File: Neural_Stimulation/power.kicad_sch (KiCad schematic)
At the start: 16 parts, among them U3 LTC3035EDDBPBF, U4 LTC3035EDDBPBF

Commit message: Added level shifters
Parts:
- added C26: 0.1uF, symbol Device:C
- added R24: 100, symbol Device:R
- added R25: 50m, symbol Device:R
- added R27: 10k, symbol Device:R
- added R28: 500m, symbol Device:R
- added U5: LT6106, Package_TO_SOT_SMD:SOT-23-5, symbol Amplifier_Current:LT6106
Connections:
- net GND: now also C26.2, R27.1, U5.2 (V-)
- net +3V3: now reaches C25.1, R20.1, U4.5 (OUT)
- net +1V8: now reaches C23.1, R22.1, U3.5 (OUT)
- new net: R24.1, R25.1, R28.1, U5.5 (V+)
- new net: C26.1, R25.2, R28.2, U5.4 (+)
- new net: R24.2, U5.3 (-)
- new net VDD_ISENSE: R27.2, U5.1
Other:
- note added: "LDO GENERATING VDD FOR CSI040"
- note added: "LDO GENERATING VDD FOR MCU"
- moved on the sheet: C23, R22

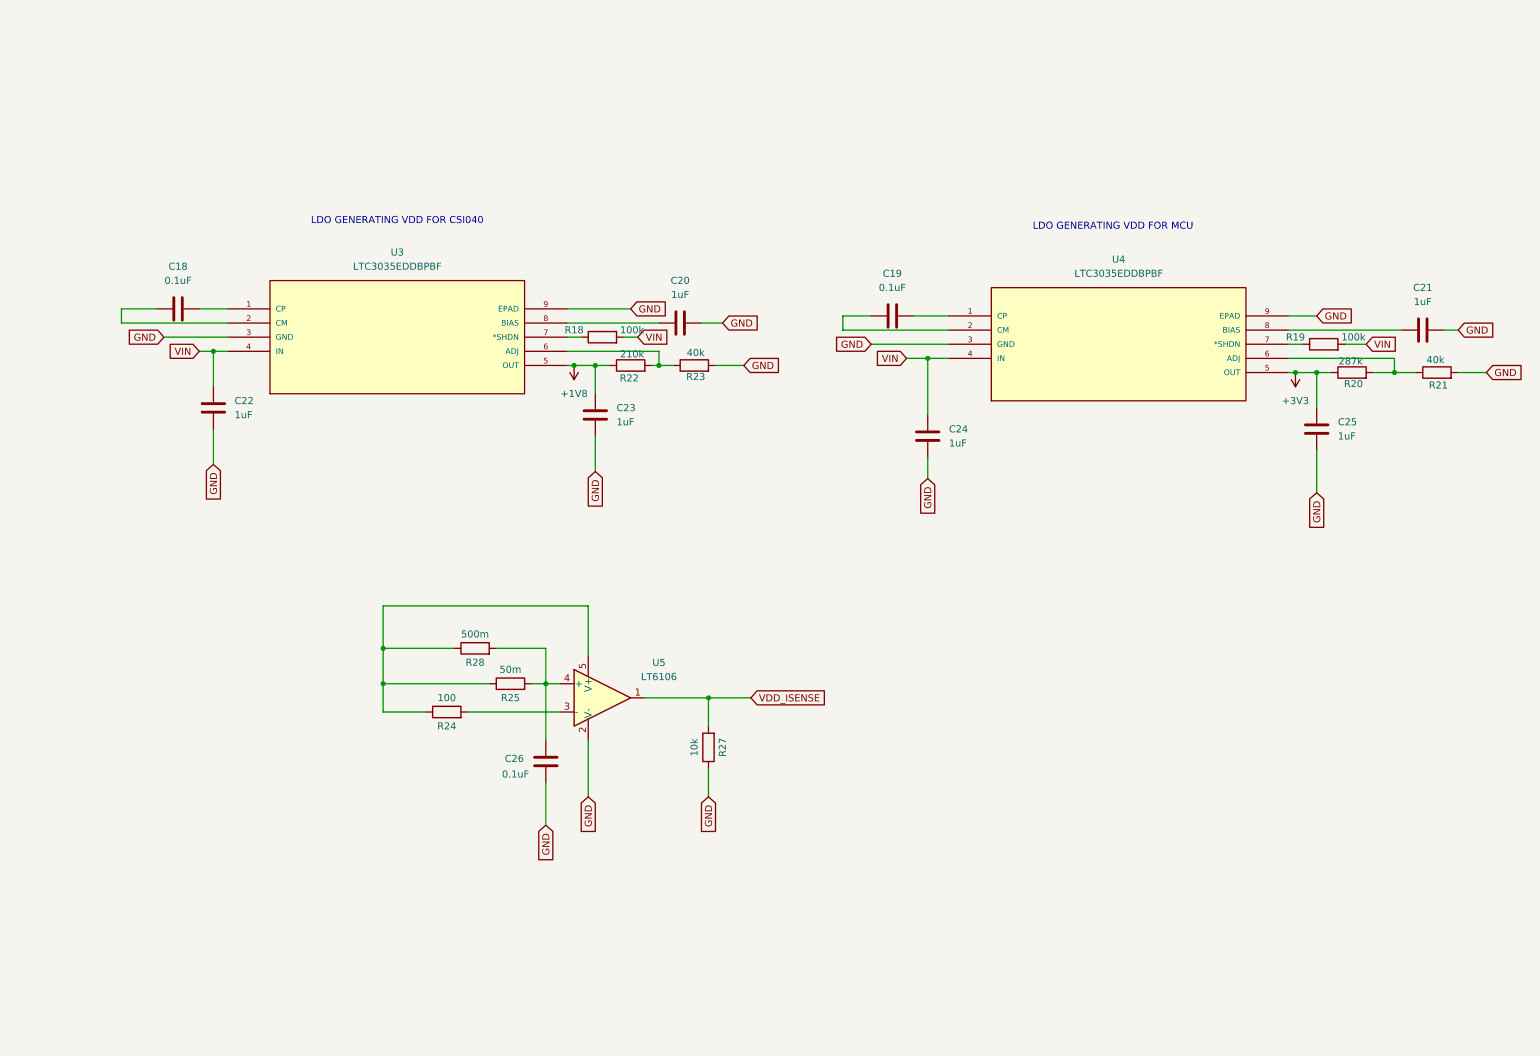
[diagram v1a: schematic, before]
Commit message: Added boost converter for generating VMAX
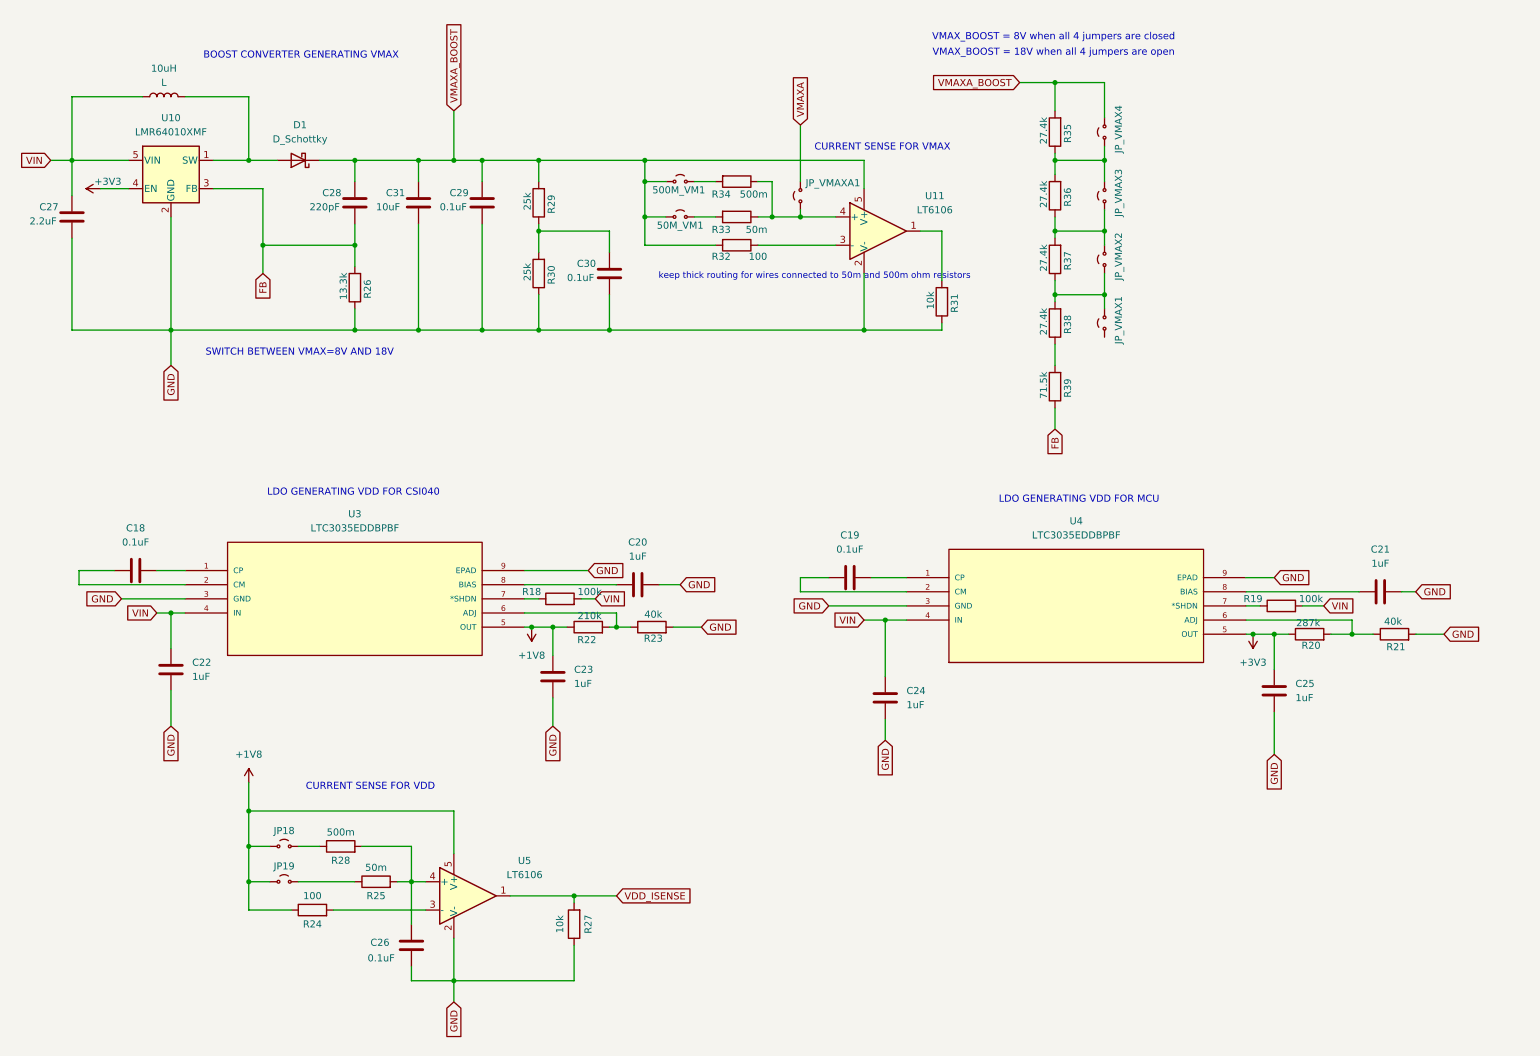
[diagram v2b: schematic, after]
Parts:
- added 10uH: L, symbol Device:L
- added 500M_VM1, 50M_VM1, JP18, JP19, JP_VMAX1, JP_VMAX2, JP_VMAX3, JP_VMAX4, JP_VMAXA1: Jumper_2_Small_Open, symbol Jumper:Jumper_2_Small_Open
- added C27: 2.2uF, symbol Device:C
- added C28: 220pF, symbol Device:C
- added C29, C30: 0.1uF, symbol Device:C
- added C31: 10uF, symbol Device:C
- added D1: D_Schottky, symbol Device:D_Schottky
- added R26: 13.3k, symbol Device:R
- added R29, R30: 25k, symbol Device:R
- added R31: 10k, symbol Device:R
- added R32: 100, symbol Device:R
- added R33: 50m, symbol Device:R
- added R34: 500m, symbol Device:R
- added R35, R36, R37, R38: 27.4k, symbol Device:R
- added R39: 71.5k, symbol Device:R
- added U10: LMR64010XMF, Package_TO_SOT_SMD:SOT-23-5, symbol Regulator_Switching:LMR64010XMF
- added U11: LT6106, Package_TO_SOT_SMD:SOT-23-5, symbol Amplifier_Current:LT6106
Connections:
- net +1V8: now also R24.1, U5.5 (V+), JP18.1 (A), JP19.1 (A)
- net +3V3: now also U10.4 (EN)
- net GND: now also C27.1, C29.1, C30.1, C31.1, R26.1, R30.1, R31.1, U10.2 (GND), U11.2 (V-)
- net VIN: now also 10uH.1, C27.2, U10.5 (VIN)
- new net: C30.2, R29.1, R30.2
- new net: JP_VMAXA1.1 (A), R33.1, R34.1, U11.4 (+)
- new net: 50M_VM1.2 (B), R33.2
- new net: JP_VMAX3.2 (B), JP_VMAX4.1 (A), R35.1, R36.2
- new net: JP_VMAX1.2 (B), JP_VMAX2.1 (A), R37.1, R38.2
- new net: R31.2, U11.1
- new net: 500M_VM1.2 (B), R34.2
- new net: JP18.2 (B), R28.1
- new net: 10uH.2, D1.2 (A), U10.1 (SW)
- new net: JP_VMAX2.2 (B), JP_VMAX3.1 (A), R36.1, R37.2
- new net: R38.1, R39.2
- new net: JP19.2 (B), R25.1
- new net: R32.1, U11.3 (-)
- new net FB: C28.1, R26.2, R39.1, U10.3 (FB)
- new net VMAXA: JP_VMAXA1.2 (B)
- new net VMAXA_BOOST: 500M_VM1.1 (A), 50M_VM1.1 (A), C28.2, C29.2, C31.2, D1.1 (K), JP_VMAX4.2 (B), R29.2, R32.2, R35.2, U11.5 (V+)
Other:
- note added: "BOOST CONVERTER GENERATING VMAX"
- note added: "CURRENT SENSE FOR VDD"
- note added: "CURRENT SENSE FOR VMAX"
- note added: "SWITCH BETWEEN VMAX=8V AND 18V"
- note added: "VMAX_BOOST = 18V when all 4 jumpers are open"
- note added: "VMAX_BOOST = 8V when all 4 jumpers are closed"
- note added: "keep thick routing for wires connected to 50m and 500m ohm resistors"
- moved on the sheet: C18, C19, C20, C21, C22, C23, C24, C25, C26, R18, R19, R20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

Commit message: Added VREF Connections
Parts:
- added JP_VREFA: Jumper_2_Small_Open, symbol Jumper:Jumper_2_Small_Open
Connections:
- net at C30.2, R29.1, R30.2: now also JP_VREFA.2 (B)
- new net VREF_A: JP_VREFA.1 (A)
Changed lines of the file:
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@@
 	)
 	(junction
+		(at 119.38 50.8)
+		(diameter 0)
+		(color 0 0 0 0)
+	)
+	(junction
 		(at 96.52 68.58)
 		(diameter 0)
@@
 	(wire
 		(pts
+			(xy 119.38 31.75) (xy 119.38 41.91)
+		)
+		(stroke
+			(width 0)
+			(type default)
+		)
+	)
+	(wire
+		(pts
 			(xy 19.05 38.1) (xy 22.86 38.1)
 		)
@@
 	(wire
 		(pts
+			(xy 119.38 46.99) (xy 119.38 50.8)
+		)
+		(stroke
+			(width 0)
+			(type default)
+		)
+	)
+	(wire
+		(pts
 			(xy 30.48 111.76) (xy 24.13 111.76)
 		)
@@
 	(wire
 		(pts
-			(xy 119.38 50.8) (xy 106.68 50.8)
+			(xy 106.68 50.8) (xy 119.38 50.8)
 		)
 		(stroke
@@
 		)
 	)
+	(global_label "VREF_A"
+		(shape input)
+		(at 119.38 31.75 90)
+		(fields_autoplaced yes)
+		(effects
+			(font
+				(size 1.27 1.27)
+			)
+			(justify left)
+		)
+		(property "Intersheetrefs" "${INTERSHEET_REFS}"
+			(at 119.38 22.1124 90)
+			(effects
+				(font
+					(size 1.27 1.27)
+				)
+				(justify left)
+				(hide yes)
+			)
+		)
+	)
 	(global_label "GND"
 		(shape input)
@@
 					(unit 1)
 				)
+			)
+		)
+	)
+	(symbol
+		(lib_id "Jumper:Jumper_2_Small_Open")
+		(at 119.38 44.45 270)
+		(unit 1)
+		(exclude_from_sim yes)
+		(in_bom yes)
+		(on_board yes)
+		(dnp no)
+		(property "Reference" "JP_VREFA"
+			(at 122.174 44.45 0)
+			(effects
+				(font
+					(size 1.27 1.27)
+				)
+			)
+		)
+		(property "Value" "Jumper_2_Small_Open"
+			(at 123.19 44.45 0)
+			(effects
+				(font
+					(size 1.27 1.27)
+				)
+				(hide yes)
+			)
+		)
+		(property "Footprint" ""
+			(at 119.38 44.45 0)
+			(effects
+				(font
+					(size 1.27 1.27)
+				)
+				(hide yes)
+			)
+		)
+		(property "Datasheet" "~"
+			(at 119.38 44.45 0)
+			(effects
+				(font
+					(size 1.27 1.27)
+				)
+				(hide yes)
+			)
+		)
+		(property "Description" "Jumper, 2-pole, small symbol, open"
+			(at 119.38 44.45 0)
+			(effects
+				(font
+					(size 1.27 1.27)
+				)
+				(hide yes)
+			)
+		)
+		(pin "1"
+		)
+		(pin "2"
+		)
+		(instances
+			(project "NeuralStimBoard.kicad_sym"
+				(path "/0df850d8-90a2-4d89-b281-e26bc82d6cd9/2af15af9-f56a-408a-9186-69deac584b7e"
+					(reference "JP_VREFA")
+					(unit 1)
+				)

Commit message: Added VDD connections to CSI040
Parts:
- added JP_VDD: Jumper_2_Small_Open, symbol Jumper:Jumper_2_Small_Open
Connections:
- net at C26.1, R25.2, R28.2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: now also JP_VDD.1 (A)
- new net VDD: JP_VDD.2 (B)
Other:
- moved on the sheet: C26, R25
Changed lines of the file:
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@@
 	)
 	(junction
+		(at 82.55 167.64)
+		(diameter 0)
+		(color 0 0 0 0)
+	)
+	(junction
+		(at 85.09 167.64)
+		(diameter 0)
+		(color 0 0 0 0)
+	)
+	(junction
+		(at 54.61 151.13)
+		(diameter 0)
+		(color 0 0 0 0)
+	)
+	(junction
 		(at 22.86 38.1)
 		(diameter 0)
@@
 	)
 	(junction
-		(at 83.82 167.64)
-		(diameter 0)
-		(color 0 0 0 0)
-	)
-	(junction
 		(at 234.95 123.19)
 		(diameter 0)
@@
 	)
 	(junction
-		(at 54.61 154.94)
-		(diameter 0)
-		(color 0 0 0 0)
-	)
-	(junction
 		(at 85.09 68.58)
 		(diameter 0)
@@
 	(wire
 		(pts
-			(xy 91.44 185.42) (xy 83.82 185.42)
+			(xy 91.44 185.42) (xy 82.55 185.42)
 		)
 		(stroke
@@
 	(wire
 		(pts
-			(xy 54.61 149.86) (xy 54.61 154.94)
+			(xy 54.61 146.05) (xy 54.61 151.13)
 		)
 		(stroke
@@
 	(wire
 		(pts
-			(xy 91.44 154.94) (xy 91.44 162.56)
+			(xy 91.44 151.13) (xy 91.44 162.56)
 		)
 		(stroke
@@
 	(wire
 		(pts
-			(xy 54.61 154.94) (xy 54.61 161.29)
+			(xy 233.68 113.03) (xy 238.76 113.03)
 		)
 		(stroke
@@
 	(wire
 		(pts
-			(xy 233.68 113.03) (xy 238.76 113.03)
+			(xy 166.37 113.03) (xy 172.72 113.03)
 		)
 		(stroke
@@
 	(wire
 		(pts
-			(xy 166.37 113.03) (xy 172.72 113.03)
+			(xy 101.6 170.18) (xy 113.03 170.18)
 		)
 		(stroke
@@
 	(wire
 		(pts
-			(xy 101.6 170.18) (xy 113.03 170.18)
+			(xy 96.52 38.1) (xy 91.44 38.1)
 		)
 		(stroke
@@
 	(wire
 		(pts
-			(xy 96.52 38.1) (xy 91.44 38.1)
+			(xy 54.61 161.29) (xy 54.61 167.64)
 		)
 		(stroke
@@
 	(wire
 		(pts
-			(xy 54.61 161.29) (xy 54.61 167.64)
+			(xy 82.55 167.64) (xy 85.09 167.64)
 		)
 		(stroke
@@
 	(wire
 		(pts
-			(xy 63.5 167.64) (xy 73.66 167.64)
+			(xy 63.5 167.64) (xy 72.39 167.64)
 		)
 		(stroke
@@
 	(wire
 		(pts
+			(xy 54.61 151.13) (xy 54.61 161.29)
+		)
+		(stroke
+			(width 0)
+			(type default)
+		)
+	)
+	(wire
+		(pts
 			(xy 119.38 54.61) (xy 119.38 50.8)
 		)
@@
 	(wire
 		(pts
-			(xy 83.82 167.64) (xy 83.82 175.26)
+			(xy 82.55 167.64) (xy 82.55 175.26)
 		)
 		(stroke
@@
 	(wire
 		(pts
-			(xy 83.82 185.42) (xy 83.82 182.88)
+			(xy 82.55 185.42) (xy 82.55 182.88)
 		)
 		(stroke
@@
 	(wire
 		(pts
-			(xy 83.82 167.64) (xy 86.36 167.64)
+			(xy 134.62 41.91) (xy 138.43 41.91)
 		)
 		(stroke
@@
 	(wire
 		(pts
-			(xy 134.62 41.91) (xy 138.43 41.91)
+			(xy 168.91 130.81) (xy 168.91 120.65)
 		)
 		(stroke
@@
 	(wire
 		(pts
-			(xy 168.91 130.81) (xy 168.91 120.65)
+			(xy 31.75 116.84) (xy 43.18 116.84)
 		)
 		(stroke
@@
 	(wire
 		(pts
-			(xy 31.75 116.84) (xy 43.18 116.84)
+			(xy 130.81 121.92) (xy 135.89 121.92)
 		)
 		(stroke
@@
 	(wire
 		(pts
-			(xy 130.81 121.92) (xy 135.89 121.92)
+			(xy 85.09 161.29) (xy 85.09 167.64)
 		)
 		(stroke
@@
 	(wire
 		(pts
+			(xy 85.09 167.64) (xy 86.36 167.64)
+		)
+		(stroke
+			(width 0)
+			(type default)
+		)
+	)
+	(wire
+		(pts
 			(xy 208.28 30.48) (xy 208.28 24.13)
 		)
@@
 	(wire
 		(pts
-			(xy 74.93 161.29) (xy 83.82 161.29)
+			(xy 74.93 161.29) (xy 82.55 161.29)
 		)
 		(stroke
@@
 	(wire
 		(pts
-			(xy 83.82 161.29) (xy 83.82 167.64)
+			(xy 82.55 161.29) (xy 82.55 167.64)
 		)
 		(stroke
@@
 	(wire
 		(pts
+			(xy 85.09 148.59) (xy 85.09 156.21)
+		)
+		(stroke
+			(width 0)
+			(type default)
+		)
+	)
+	(wire
+		(pts
 			(xy 40.64 68.58) (xy 73.66 68.58)
 		)
@@
 	(wire
 		(pts
-			(xy 54.61 154.94) (xy 91.44 154.94)
+			(xy 54.61 151.13) (xy 91.44 151.13)
 		)
 		(stroke
@@
 	(wire
 		(pts
-			(xy 81.28 167.64) (xy 83.82 167.64)
+			(xy 80.01 167.64) (xy 82.55 167.64)
 		)
 		(stroke
@@
 	(text "CURRENT SENSE FOR VDD"
 		(exclude_from_sim no)
-		(at 76.454 150.622 0)
+		(at 69.596 146.558 0)
 		(effects
 			(font
@@
 		)
 	)
+	(global_label "VDD"
+		(shape input)
+		(at 85.09 148.59 90)
+		(fields_autoplaced yes)
+		(effects
+			(font
+				(size 1.27 1.27)
+			)
+			(justify left)
+		)
+		(property "Intersheetrefs" "${INTERSHEET_REFS}"
+			(at 85.09 141.9762 90)
+			(effects
+				(font
+					(size 1.27 1.27)
+				)
+				(justify left)
+				(hide yes)
+			)
+		)
+	)
 	(global_label "GND"
 		(shape input)
@@
 	)
 	(symbol
+		(lib_id "Jumper:Jumper_2_Small_Open")
+		(at 85.09 158.75 90)
+		(unit 1)
+		(exclude_from_sim yes)
+		(in_bom yes)
+		(on_board yes)
+		(dnp no)
+		(property "Reference" "JP_VDD"
+			(at 79.756 158.242 90)
+			(effects
+				(font
+					(size 1.27 1.27)
+				)
+			)
+		)
+		(property "Value" "Jumper_2_Small_Open"
+			(at 81.28 158.75 0)
+			(effects
+				(font
+					(size 1.27 1.27)
+				)
+				(hide yes)
+			)
+		)
+		(property "Footprint" ""
+			(at 85.09 158.75 0)
+			(effects
+				(font
+					(size 1.27 1.27)
+				)
+				(hide yes)
+			)
+		)
+		(property "Datasheet" "~"
+			(at 85.09 158.75 0)
+			(effects
+				(font
+					(size 1.27 1.27)
+				)
+				(hide yes)
+			)
+		)
+		(property "Description" "Jumper, 2-pole, small symbol, open"
+			(at 85.09 158.75 0)
+			(effects
+				(font
+					(size 1.27 1.27)
+				)
+				(hide yes)
+			)
+		)
+		(pin "1"
+		)
+		(pin "2"
+		)
+		(instances
+			(project "NeuralStimBoard.kicad_sym"
+				(path "/0df850d8-90a2-4d89-b281-e26bc82d6cd9/2af15af9-f56a-408a-9186-69deac584b7e"
+					(reference "JP_VDD")
+					(unit 1)
+				)
+			)
+		)
+	)
+	(symbol
 		(lib_id "Device:R")
 		(at 106.68 58.42 180)
@@
 	(symbol
 		(lib_id "Device:C")
-		(at 83.82 179.07 0)
+		(at 82.55 179.07 0)
 		(unit 1)
 		(exclude_from_sim no)
@@
 		(dnp no)
 		(property "Reference" "C26"
-			(at 76.454 178.562 0)
+			(at 75.184 178.562 0)
 			(effects
 				(font
@@
 		)
 		(property "Value" "0.1uF"
-			(at 75.946 181.356 0)
+			(at 74.676 181.356 0)
 			(effects
 				(font
@@
 		)
 		(property "Footprint" ""
-			(at 84.7852 182.88 0)
+			(at 83.5152 182.88 0)
 			(effects
 				(font
@@
 		)
 		(property "Datasheet" "~"
-			(at 83.82 179.07 0)
+			(at 82.55 179.07 0)
 			(effects
 				(font
@@
 		)
 		(property "Description" "Unpolarized capacitor"
-			(at 83.82 179.07 0)
+			(at 82.55 179.07 0)
 			(effects
 				(font
@@
 	(symbol
 		(lib_id "power:+1V8")
-		(at 54.61 149.86 0)
+		(at 54.61 146.05 0)
 		(unit 1)
 		(exclude_from_sim no)
@@
 		(dnp no)
 		(property "Reference" "#PWR06"
-			(at 54.61 153.67 0)
+			(at 54.61 149.86 0)
 			(effects
 				(font
@@
 		)
 		(property "Value" "+1V8"
-			(at 54.61 144.78 0)
+			(at 54.61 140.97 0)
 			(effects
 				(font
@@
 		)
 		(property "Footprint" ""
-			(at 54.61 149.86 0)
+			(at 54.61 146.05 0)
 			(effects
 				(font
@@
 		)
 		(property "Datasheet" ""
-			(at 54.61 149.86 0)
+			(at 54.61 146.05 0)
 			(effects
 				(font
@@
 		)
 		(property "Description" "Power symbol creates a global label with name \"+1V8\""
-			(at 54.61 149.86 0)
+			(at 54.61 146.05 0)
 			(effects
 				(font
@@
 	(symbol
 		(lib_id "Device:R")
-		(at 77.47 167.64 90)
+		(at 76.2 167.64 90)
 		(unit 1)
 		(exclude_from_sim no)
@@
 		(dnp no)
 		(property "Reference" "R25"
-			(at 77.47 170.18 90)
+			(at 76.2 170.18 90)
 			(effects
 				(font
@@
 		)
 		(property "Value" "50m"
-			(at 77.47 165.1 90)
+			(at 76.2 165.1 90)
 			(effects
 				(font
@@
 		)
 		(property "Footprint" ""
-			(at 77.47 169.418 90)
+			(at 76.2 169.418 90)
 			(effects
 				(font
@@
 		)
 		(property "Datasheet" "~"
-			(at 77.47 167.64 0)
+			(at 76.2 167.64 0)
 			(effects
 				(font
@@
 		)
 		(property "Description" "Resistor"
-			(at 77.47 167.64 0)
+			(at 76.2 167.64 0)
 			(effects
 				(font

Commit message: Added INT, TRIG, ATEST and RSTN pin circuits
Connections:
- net at JP_VMAX1.1 (A): now also R38.1, R39.2
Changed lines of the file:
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@@
+	)
+	(junction
+		(at 199.39 73.66)
+		(diameter 0)
+		(color 0 0 0 0)
 	)
 	(junction
@@
 	(wire
 		(pts
+			(xy 208.28 73.66) (xy 199.39 73.66)
+		)
+		(stroke
+			(width 0)
+			(type default)
+		)
+	)
+	(wire
+		(pts
 			(xy 234.95 123.19) (xy 238.76 123.19)
 		)
@@
 	(wire
 		(pts
-			(xy 199.39 71.12) (xy 199.39 74.93)
+			(xy 199.39 71.12) (xy 199.39 73.66)
 		)
 		(stroke
@@
 	(wire
 		(pts
+			(xy 208.28 69.85) (xy 208.28 73.66)
+		)
+		(stroke
+			(width 0)
+			(type default)
+		)
+	)
+	(wire
+		(pts
 			(xy 125.73 48.26) (xy 125.73 41.91)
 		)
@@
 		)
 		(stroke
+			(width 0)
+			(type default)
+		)
+	)
+	(wire
+		(pts
+			(xy 199.39 73.66) (xy 199.39 74.93)
+		)
+		(stroke
